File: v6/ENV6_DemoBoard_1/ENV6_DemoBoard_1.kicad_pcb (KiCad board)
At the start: 4 copper layers, 73 x 45 mm, 125 parts, among them IC301 LP873300RHDTQ1, J201 MEM2052-00-195-00-A, J401 Pico Debugger (SWD), J402 Conn_01x04_Pin, J501 Conn_02x16_Odd_Even, J502 Conn_02x04_Odd_Even, J503 Conn_02x16_Odd_Even, J504 Conn_02x04_Odd_Even, J505 Conn_02x16_Odd_Even, U201 PAC1954x-x4MX, U202 PAC1954x-x4MX, U203 PAC1954x-x4MX, U301 BQ25188, U302 TPSM8310x, U401 RP2354B, U402 Pi-Radio, U403 W25Q16JVUXIQ, Y401 KX7_QRZ

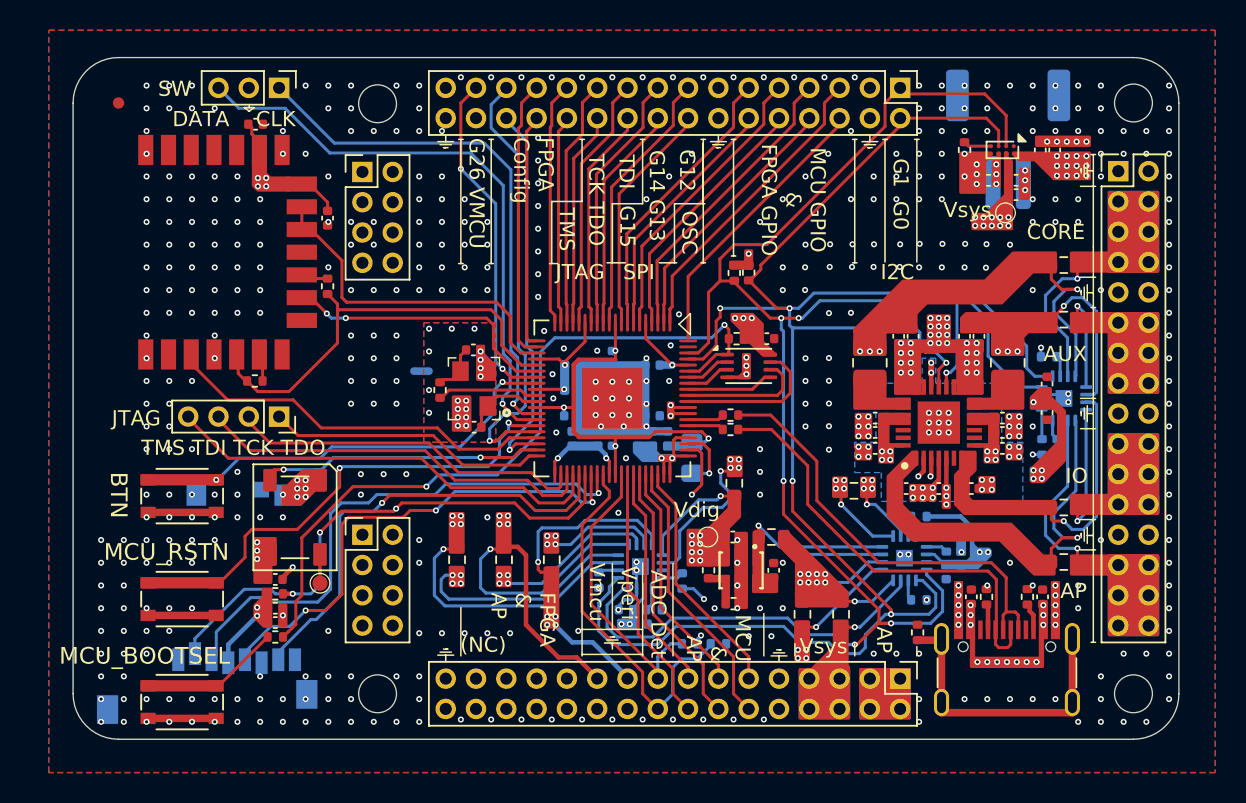
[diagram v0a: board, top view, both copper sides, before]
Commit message: SPartan7Board and new Symbol and Footprint
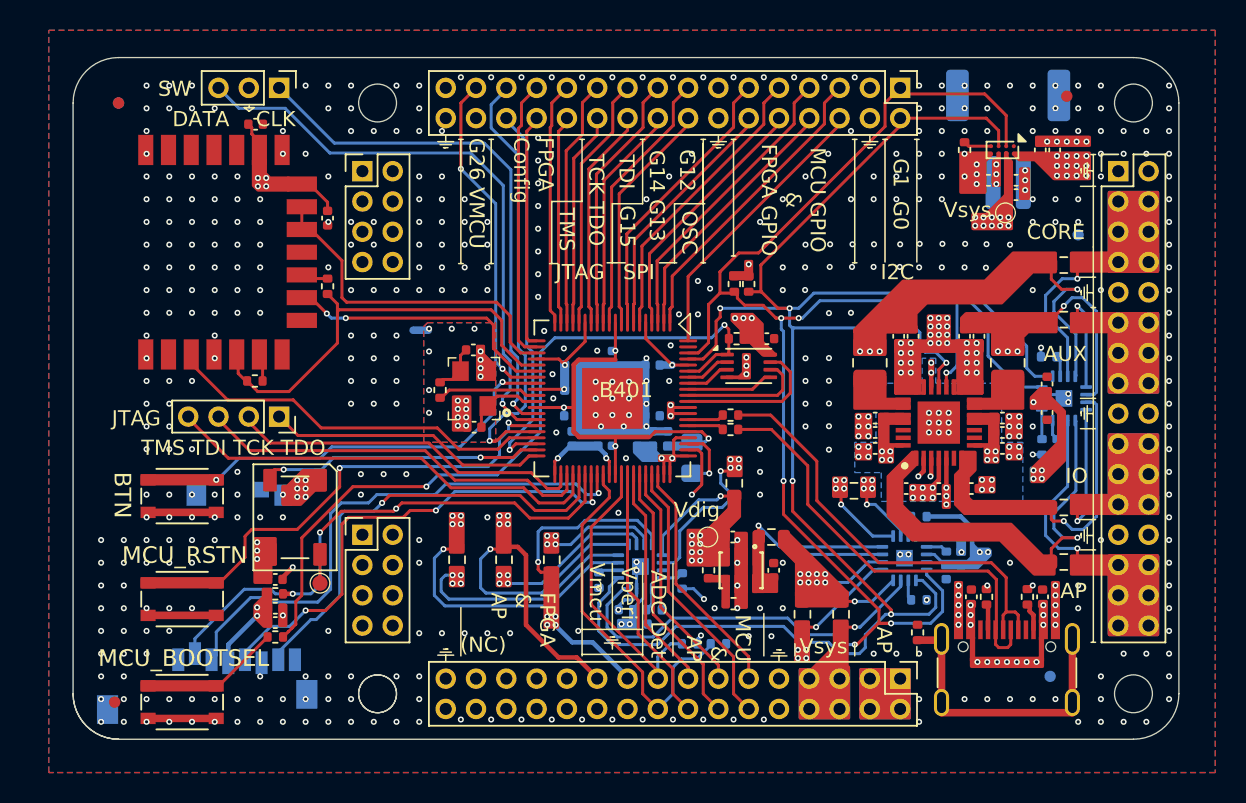
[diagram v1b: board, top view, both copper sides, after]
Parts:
- removed H501, H502, H504: MountingHole, MountingHole:MountingHole_2.5mm
- removed J501, J503, J505: Conn_02x16_Odd_Even, Connector_PinHeader_2.00mm:PinHeader_2x16_P2.00mm_Vertical
- removed J502, J504: Conn_02x04_Odd_Even, Connector_PinHeader_2.00mm:PinHeader_2x04_P2.00mm_Vertical
- added B401: ~, ENv6_Custom_Footprints:BaseBoard_ENv6, F.Cu at (161.1, 105.3)
- added REF**: Fiducial_0.75mm_Mask1.5mm, maker:Fiducial_0.75mm_Mask1.5mm, F.Cu at (190.2, 85.3)
- added REF**: Fiducial_0.75mm_Mask1.5mm, maker:Fiducial_0.75mm_Mask1.5mm, F.Cu at (127.3, 125.3)
- added REF**: Fiducial_0.75mm_Mask1.5mm, maker:Fiducial_0.75mm_Mask1.5mm, B.Cu at (127.6, 85.8)
- added REF**: Fiducial_0.75mm_Mask1.5mm, maker:Fiducial_0.75mm_Mask1.5mm, B.Cu at (189.1, 123.7)
- added REF**: Fiducial_0.75mm_Mask1.5mm, maker:Fiducial_0.75mm_Mask1.5mm, B.Cu at (190.9, 94.5)
- C201, C203, C205, C208, C302, C303, C305, C307, C308, C309, C310, C311, C312, C313, C314, C315, C316, C317, C318, C319, C320, C321, C322, C411, C412: value 10u -> 1u
- C202, C204, C206, C207, C301, C304, C306, C401, C402, C403, C404, C405, C406, C407, C408, C409, C410, C414, C415, C416: value 100n -> 1u
- L301, L302: value 0.47uH -> 0.47u
- moved NT401 2.70 mm to (147.6, 100.8)
- moved R401 0.75 mm to (169.2, 97.8)
- moved R402 0.73 mm to (168.2, 97.8)
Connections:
- U401 pad 20: FPGA_RST -> FPGA_CFG_1
- U401 pad 21: POR_EN -> FPGA_CFG_2
- U401 pad 22: CFG_DONE -> FPGA_CFG_3
- U401 pad 36: CFG_Extra -> FPGA_CFG_5
- U401 pad 38: CFG_FAILED_N -> FPGA_CFG_4
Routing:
- net FPGA_CFG_5: track 0.00 -> 29.8 mm, vias 0 -> 1
- net CFG_Extra: track 29.8 -> 0.00 mm, vias 1 -> 0
- net FPGA_CFG_4: track 0.00 -> 25.2 mm, vias 0 -> 2
- net CFG_FAILED_N: track 25.2 -> 0.00 mm, vias 1 -> 0
- net FPGA_CFG_3: track 0.00 -> 18.6 mm
- net CFG_DONE: track 18.6 -> 0.00 mm
- net FPGA_RST: track 16.1 -> 0.00 mm
- net FPGA_CFG_1: track 0.00 -> 16.1 mm
- net POR_EN: track 15.5 -> 0.00 mm
- net FPGA_CFG_2: track 0.00 -> 15.5 mm
- net AGND: track 3.15 -> 3.86 mm
- net GP1/I2C0_SCL: track 122.2 -> 121.6 mm, vias 6 -> 7
- net unconnected-(B401-PadB28): vias 0 -> 1
- net VDDD_MCU: vias 15 -> 16
- net GND: vias 514 -> 513
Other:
- board text removed: "Add a seperate filled zone for GND at the oscillator"
- board text removed: "Add fiducials from maker lib into each corner on bottom and top layer (helps the assembling machine to set the devices precisely)"
- board text removed: "If we want to have round corners, we have to do it manually. I can do it at the end"
- board text removed: "You can also use Layer In1.Cu for the power distribution (currently we have enough space for GND)"

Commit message: Fix small errors for the design
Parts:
- removed the C201 at (162.1, 120.2)
- removed the C202 at (161.1, 119.2)
- removed C205, C206: 1u, Capacitor_SMD:C_0402_1005Metric
- removed H503: MountingHole, MountingHole:MountingHole_2.5mm
- removed the R205 at (159.3, 117.3)
- removed the R206 at (162.9, 119.2)
- removed the R207 at (164.8, 117.3)
- removed the R208 at (190.0, 112.5)
- removed R209, R210, R211, R215, R216, R217, R218: 1R, Resistor_SMD:R_0603_1608Metric
- removed R219: 100k, Resistor_SMD:R_0402_1005Metric
- removed R220: 750R, Resistor_SMD:R_0402_1005Metric
- removed R221: 10k, Resistor_SMD:R_0402_1005Metric
- removed REF** (x6): Fiducial_0.75mm_Mask1.5mm, maker:Fiducial_0.75mm_Mask1.5mm
- removed U202, U203: PAC1954x-x4MX, Package_DFN_QFN:VQFN-16-1EP_3x3mm_P0.5mm_EP1.1x1.1mm
- J_BATT301: footprint Connector_JST:JST_PH_S2B-PH-SM4-TB_1x02-1MP_P2.00mm_Horizontal -> connectors:JST_PH_S2B-PH-SM4-TB_1x02-1MP_P2.00mm_Horizontal
- U201: value PAC1954x-x4MX -> PAC1954T-E4Mx; footprint Package_DFN_QFN:VQFN-16-1EP_3x3mm_P0.5mm_EP1.1x1.1mm -> sensors:VQFN-16-1EP_3x3mm_P0.5mm_EP1.1x1.1mm
- moved R203 39.9 mm to (189.9, 116.3), turned to 0 degrees
- moved R201 39.1 mm to (190.0, 96.3), turned to 0 degrees
- moved R204 37.1 mm to (190.0, 112.5), turned to 0 degrees
- moved U201 30.1 mm to (190.0, 105.3), turned to 0 degrees
- moved R202 24.2 mm to (190.0, 100.3), turned to 0 degrees
- moved J_BATT301 0.37 mm to (186.6, 87.9)
- renumbered C203 to C201, C204 to C202, C207 to C203, C208 to C204, C308 to C301, C310 to C302, C309 to C303, C311 to C304, C312 to C305, C313 to C306, C314 to C307, C301 to C308, C302 to C309, C315 to C310, C316 to C311, C317 to C312, C318 to C313, C319 to C314, C320 to C315, C303 to C316, C305 to C317, C307 to C318, C321 to C319, C304 to C320, C306 to C321, C404 to C401, C414 to C402, C405 to C403, C406 to C404, C407 to C405, C401 to C406, C408 to C407, C402 to C408, C411 to C410, C412 to C411, C417 to C412, C403 to C413, C410 to C414, C418 to C415, C413 to C416, C415 to C417, C416 to C418, R212 to R205, R213 to R206, R214 to R207, R222 to R208, R303 to R301, R301 to R302, R302 to R303, R410 to R401, R411 to R402, R408 to R403, R407 to R404, R409 to R405, R403 to R406, R404 to R407, R401 to R408, R402 to R409, R405 to R410, R406 to R411, S403 to S401, S401 to S402, S402 to S403, U403 to U401, U401 to U402, U402 to U403
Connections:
- B401 pad A30: VDDD_MCU -> VDDD_FLASH
- B401 pad B19: VDDD_PERI -> VDDD_FLASH
- B401 pad B21: VDDD_MCU -> VDDD_FLASH
- B401 pad B5: VSYS_EX -> VDIG_IN
- B401 pad B6: VSYS_EX -> VDIG_IN
- B401 pad B7: VSYS_EX -> VDIG_IN
- B401 pad B8: VSYS_EX -> VDIG_IN
- C201 pad 2: VDDD_PERI -> VDDD_FLASH
- C202 pad 2: VDDD_PERI -> VDDD_FLASH
- C203 pad 2: VDDD_PERI -> VDDD_FLASH
- C204 pad 2: VDDD_PERI -> VDDD_FLASH
- C301 pad 2: VFPGA_IN -> VDIG_IN
- C302 pad 2: VFPGA_IN -> VDIG_IN
- C303 pad 2: VFPGA_IN -> VDIG_IN
- C304 pad 2: VFPGA_IN -> VDIG_IN
- C305 pad 2: VFPGA_IN -> VDIG_IN
- C306 pad 2: VFPGA_IN -> VDIG_IN
- C307 pad 2: VFPGA_IN -> VDIG_IN
- C317 pad 1: VSYS_IN -> VDIG_IN
- C321 pad 1: VSYS_IN -> VDIG_IN
- C322 pad 2: VDIG_OUT -> VDDD_FLASH
- C401 pad 2: VDDD_MCU -> VDDD_FLASH
- C403 pad 2: VDDD_MCU -> VDDD_FLASH
- C404 pad 2: VDDD_MCU -> VDDD_FLASH
- C405 pad 2: VDDD_MCU -> VDDD_FLASH
- C407 pad 2: VDDD_MCU -> VDDD_FLASH
- C409 pad 2: VDDD_MCU -> VDDD_FLASH
- C410 pad 2: VDDD_MCU -> VDDD_FLASH
- C414 pad 2: VDDD_MCU -> VDDD_FLASH
- C416 pad 1: VPERI_IN -> VDIG_IN
- C417 pad 1: VDDD_RADIO -> VDDD_FLASH
- C418 pad 1: VDDD_RADIO -> VDDD_FLASH
- D401 pad 1: VPERI_IN -> VDIG_IN
- IC301 pad 11: VFPGA_IN -> VDIG_IN
- IC301 pad 12: VFPGA_IN -> VDIG_IN
- IC301 pad 24: VFPGA_IN -> VDIG_IN
- IC301 pad 25: VFPGA_IN -> VDIG_IN
- IC301 pad 28: VFPGA_IN -> VDIG_IN
- IC301 pad 5: VFPGA_IN -> VDIG_IN
- IC301 pad 8: VFPGA_IN -> VDIG_IN
- J201 pad 4: VDDD_PERI -> VDDD_FLASH
- R201 pad 1: VDDD_PERI -> PSU_OUT1
- R201 pad 2: VDIG_OUT -> /V1
- R202 pad 1: VDDD_FLASH -> PSU_OUT2
- R202 pad 2: VDIG_OUT -> /V2
- R203 pad 1: VDDD_RADIO -> PSU_OUT3
- R203 pad 2: VDIG_OUT -> /V3
- R204 pad 1: VDDD_MCU -> PSU_OUT4
- R204 pad 2: VDIG_OUT -> /V4
- R205 pad 1: Net-(U202-ADDRSEL) -> Net-(U201-ADDRSEL)
- R206 pad 1: Net-(U202-SLOW) -> Net-(U201-SLOW)
- R207 pad 1: VDDD_PERI -> VDDD_FLASH
- R207 pad 2: Net-(U202-~{PWRDN}) -> Net-(U201-~{PWRDN})
- R208 pad 2: VDDD_PERI -> VDDD_FLASH
- R305 pad 1: VDIG_OUT -> VDDD_FLASH
- R408 pad 1: VDDD_MCU -> VDDD_FLASH
- R409 pad 1: VDDD_MCU -> VDDD_FLASH
- TP301 pad 1: VSYS_IN -> VDIG_IN
- TP302 pad 1: VDIG_OUT -> VDDD_FLASH
- U201 pad 10: VDIG_OUT -> /Peripherals/PAC_SenseP_4
- U201 pad 11: VDIG_OUT -> /Peripherals/PAC_SenseN_1
- U201 pad 12: VDDD_PERI -> /Peripherals/PAC_SenseP_1
- U201 pad 13: VDIG_OUT -> /Peripherals/PAC_SenseP_2
- U201 pad 14: VDDD_FLASH -> /Peripherals/PAC_SenseN_2
- U201 pad 2: VDDD_PERI -> VDDD_FLASH
- U201 pad 7: VDDD_RADIO -> /Peripherals/PAC_SenseN_3
- U201 pad 8: VDIG_OUT -> /Peripherals/PAC_SenseP_3
- U201 pad 9: VDDD_MCU -> /Peripherals/PAC_SenseN_4
- U301 pad B2: VSYS_IN -> VDIG_IN
- U302 pad 4: VDIG_OUT -> VDDD_FLASH
- U402 pad 15: VDDD_MCU -> VDDD_FLASH
- U402 pad 24: VDDD_MCU -> VDDD_FLASH
- U402 pad 29: VDDD_MCU -> VDDD_FLASH
- U402 pad 41: VDDD_MCU -> VDDD_FLASH
- U402 pad 5: VDDD_MCU -> VDDD_FLASH
- U402 pad 50: VDDD_MCU -> VDDD_FLASH
- U402 pad 59: VDDD_MCU -> VDDD_FLASH
- U402 pad 60: VDDD_MCU -> VDDD_FLASH
- U402 pad 61: VDDD_MCU -> VDDD_FLASH
- U402 pad 64: VDDD_MCU -> VDDD_FLASH
- U402 pad 68: VDDD_MCU -> VDDD_FLASH
- U402 pad 69: VDDD_MCU -> VDDD_FLASH
- U402 pad 76: VDDD_MCU -> VDDD_FLASH
- U403 pad 14: VDDD_RADIO -> VDDD_FLASH
- U403 pad 16: VDDD_RADIO -> VDDD_FLASH
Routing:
- net GP1/I2C0_SCL: track 121.6 -> 66.8 mm, vias 7 -> 2
- net GP0/I2C0_SDA: track 125.5 -> 71.6 mm, vias 5 -> 3
- net VDDD_MCU: track 53.5 -> 0.00 mm, vias 16 -> 0
- net VDDD_FLASH: track 10.2 -> 51.3 mm, vias 8 -> 38
- net VDDD_PERI: track 40.2 -> 0.00 mm, vias 17 -> 0
- net VDIG_OUT: track 39.3 -> 0.00 mm, vias 21 -> 0
- net VDDD_RADIO: track 27.3 -> 0.00 mm, vias 9 -> 0
- net VSYS_IN: track 22.7 -> 0.00 mm, vias 24 -> 0
- net VFPGA_IN: track 10.6 -> 0.00 mm, vias 16 -> 0
- net VPERI_IN: track 8.56 -> 0.00 mm, vias 8 -> 0
- net VSYS_EX: track 5.46 -> 0.00 mm, vias 1 -> 0
- net GND: track 32.3 -> 28.6 mm, vias 513 -> 508
- net Net-(U202-SLOW): track 1.95 -> 0.00 mm
- net ADC_Detect2: track 19.5 -> 17.9 mm
- net ADC_Detect1: track 24.8 -> 23.3 mm
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- added copper zone on In1.Cu, net VDIG_IN
- added copper zone on In2.Cu, net VDIG_IN
- removed copper zone on In1.Cu, net VDDD_MCU
- removed copper zone on In2.Cu, net VDDD_MCU
- removed copper zone on In1.Cu, net VDDD_PERI
- removed copper zone on In2.Cu, net VDDD_PERI
- removed copper zone on In1.Cu, net VDDD_RADIO
- removed copper zone on In2.Cu, net VDDD_RADIO
- removed copper zone on In1.Cu, net VDIG_OUT
- removed copper zone on In2.Cu, net VDIG_OUT
- removed copper zone on In1.Cu, net VFPGA_IN
- removed copper zone on In2.Cu, net VFPGA_IN
- removed copper zone on In1.Cu, net VPERI_IN
- removed copper zone on In2.Cu, net VPERI_IN
- removed copper zone on In1.Cu, net VSYS_IN
- removed copper zone on In2.Cu, net VSYS_IN
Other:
- board text added: "Put it on the top layer (should be enough space"
